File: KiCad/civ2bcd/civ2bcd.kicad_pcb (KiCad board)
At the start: 2 copper layers, 70 x 45 mm, 61 parts, among them J1 7-15VDC, J2 SWD, J3 CI-V (IN), J4 CI-V (OUT), J5 BCD OUTPUT 1, J6 BCD OUTPUT 2, Q1 BC817, Q2 BC817, Q3 BC817, Q4 BC817, U1 RS3002-5.0YF5, U2 CH32V003F4P6

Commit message: fix issues with civ input
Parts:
- removed Q1, Q2, Q3, Q4: BC817, Package_TO_SOT_SMD:SOT-23
- removed R3, R4: 34k, Resistor_SMD:R_1206_3216Metric
- removed the R5 at (193.5, 61.0)
- removed the R6 at (150.0, 97.0)
- removed the R7 at (184.0, 72.5)
- removed the R8 at (150.0, 90.5)
- R1: renamed from R2; value 10k -> 1k
- R15: renamed from R1; value 10k -> 1k
- moved R15 5.00 mm to (189.5, 66.5), turned to 180 degrees
- renumbered C6 to C10, C7 to C11, C3 to C4, C4 to C6, C5 to C9, J4 to J2, J2 to J3, J5 to J4, J6 to J5, J3 to J6, R18 to R19, R17 to R20, R16 to R21, R15 to R22, R22 to R5, R21 to R6, R20 to R7, R19 to R8, U2 to U1, U1 to U2
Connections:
- J2 pad 2: Net-(J4-Pin_2) -> Net-(J2-Pin_2)
- R1 pad 2: Net-(Q2-B) -> Net-(J2-Pin_2)
- R15 pad 2: Net-(Q1-B) -> CI-V
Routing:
- net GND: track 343.7 -> 300.9 mm, vias 2 -> 1
- net Net-(J2-Pin_2): track 0.00 -> 30.0 mm
- net Net-(J4-Pin_2): track 27.7 -> 0.00 mm, vias 2 -> 0
- net Net-(Q1-C): track 22.4 -> 0.00 mm, vias 2 -> 0
- net +5V: track 90.8 -> 74.8 mm
- net Net-(Q4-B): track 13.8 -> 0.00 mm, vias 2 -> 0
- net Net-(Q2-C): track 12.3 -> 0.00 mm
- net Net-(Q2-B): track 9.77 -> 0.00 mm
- net Net-(Q1-B): track 8.79 -> 0.00 mm
- net Net-(Q3-B): track 8.28 -> 0.00 mm, vias 2 -> 0
- net CI-V: track 20.8 -> 17.7 mm
- net Net-(J6-Pin_2): track 82.3 -> 80.4 mm
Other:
- board text removed: "34k"

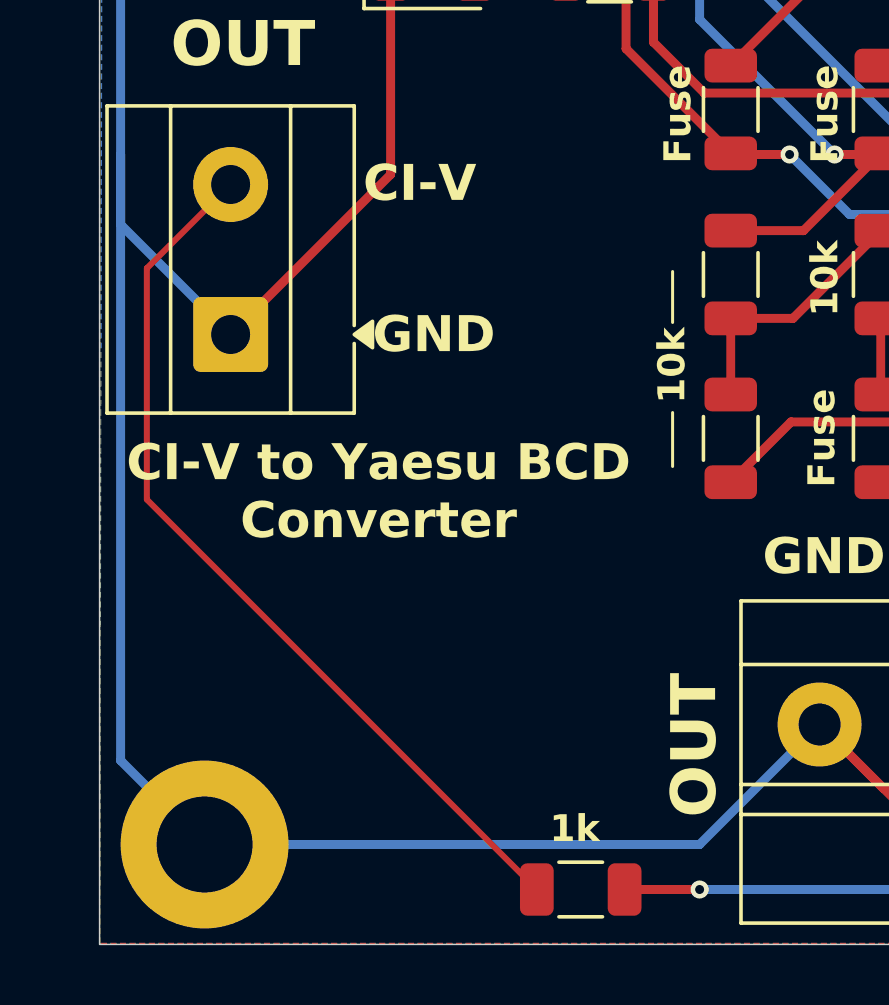
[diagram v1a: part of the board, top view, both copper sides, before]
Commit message: fix civ connection
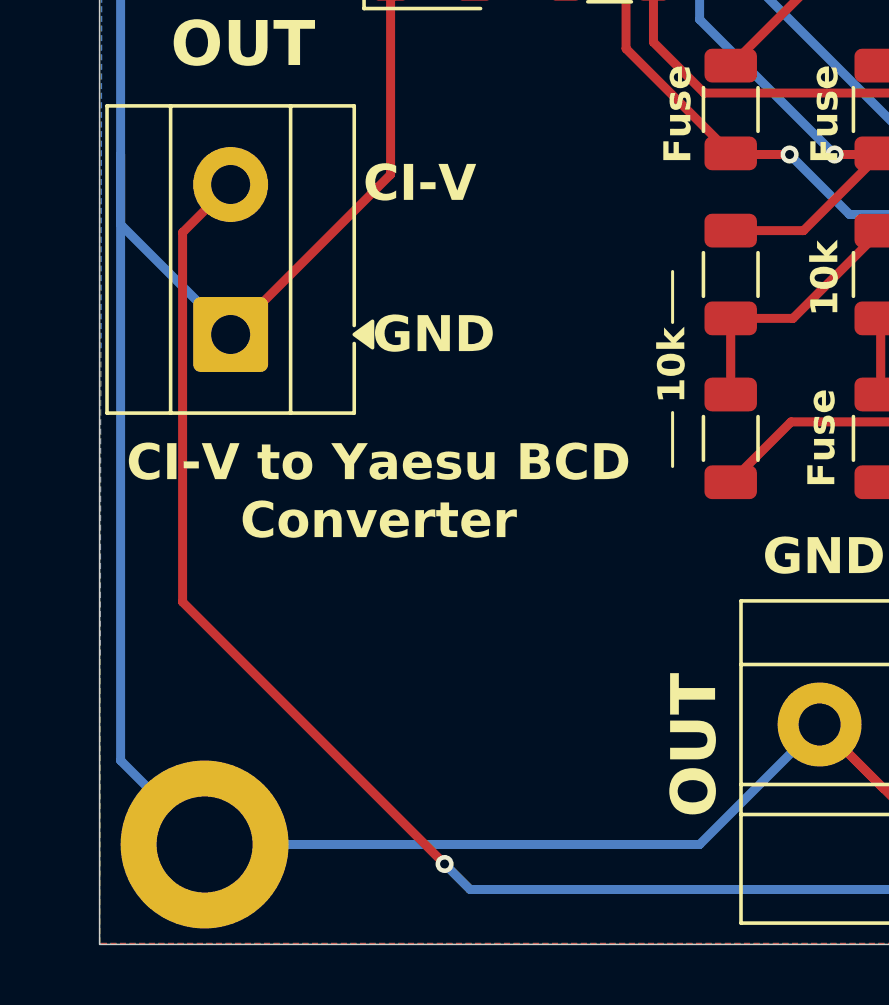
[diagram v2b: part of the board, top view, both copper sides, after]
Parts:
- removed R1: 1k, Resistor_SMD:R_1206_3216Metric
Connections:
- J6 pad 2: Net-(J6-Pin_2) -> Net-(J2-Pin_2)
- R15 pad 1: Net-(J6-Pin_2) -> Net-(J2-Pin_2)
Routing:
- net Net-(J2-Pin_2): track 30.0 -> 113.7 mm, vias 0 -> 1
- net Net-(J6-Pin_2): track 80.4 -> 0.00 mm, vias 1 -> 0
